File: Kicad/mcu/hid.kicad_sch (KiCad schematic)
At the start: 34 parts, among them IC401 MCP2221A, K401 VIN, K402 FRONT #1, K403 +5V, K404 FRONT #2, K405 SERVO LEFT, K406 USB/UART, K407 FRONT #3, K408 SERVO RIGHT, K409 FRONT #4

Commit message: TBOT MCU
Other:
- note added: "*R407, *R412: Optional, for SHARP IR Wheel"
- note removed: "*R408, *R413: Optional, for SHARP IR Wheel"
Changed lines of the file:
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@@
     (effects (font (size 1.27 1.27)) (justify right bottom))
   )
-  (text "*" (at 241.3 113.03 0)
+  (text "*" (at 236.855 101.6 0)
     (effects (font (size 1.27 1.27)) (justify left bottom))
   )
@@
     (effects (font (size 1.27 1.27)) (justify right bottom))
   )
-  (text "*" (at 180.34 113.03 0)
+  (text "*" (at 175.895 101.6 0)
     (effects (font (size 1.27 1.27)) (justify left bottom))
   )
@@
     (effects (font (size 1.27 1.27)) (justify right bottom))
   )
-  (text "*R408, *R413: Optional, for SHARP IR Wheel" (at 185.42 173.99 0)
+  (text "*R407, *R412: Optional, for SHARP IR Wheel" (at 185.42 173.99 0)
     (effects (font (size 1.27 1.27)) (justify left bottom))
   )
@@
   (symbol (lib_id "tronixio:R-1206") (at 243.84 114.3 270) (unit 1)
     (in_bom yes) (on_board yes)
-    (property "Reference" "R413" (id 0) (at 244.475 111.76 90)
+    (property "Reference" "R413" (id 0) (at 243.84 111.76 90)
       (effects (font (size 1.15 1.15)))
     )
@@
   (symbol (lib_id "tronixio:R-1206") (at 236.22 104.14 180) (unit 1)
     (in_bom yes) (on_board yes)
-    (property "Reference" "R412" (id 0) (at 238.76 100.33 0)
+    (property "Reference" "R412" (id 0) (at 240.03 100.33 0)
       (effects (font (size 1.15 1.15)))
     )
@@
   (symbol (lib_id "tronixio:R-1206") (at 175.26 104.14 180) (unit 1)
     (in_bom yes) (on_board yes)
-    (property "Reference" "R407" (id 0) (at 177.8 100.33 0)
+    (property "Reference" "R407" (id 0) (at 179.07 100.33 0)
       (effects (font (size 1.15 1.15)))
     )
@@
   (symbol (lib_id "tronixio:R-1206") (at 182.88 114.3 270) (unit 1)
     (in_bom yes) (on_board yes)
-    (property "Reference" "R408" (id 0) (at 183.515 111.76 90)
-      (effects (font (size 1.15 1.15)))
-    )
+    (property "Reference" "R408" (id 0) (at 182.88 111.76 90)
+      (effects (font (size 1.15 1.15)))
+    )

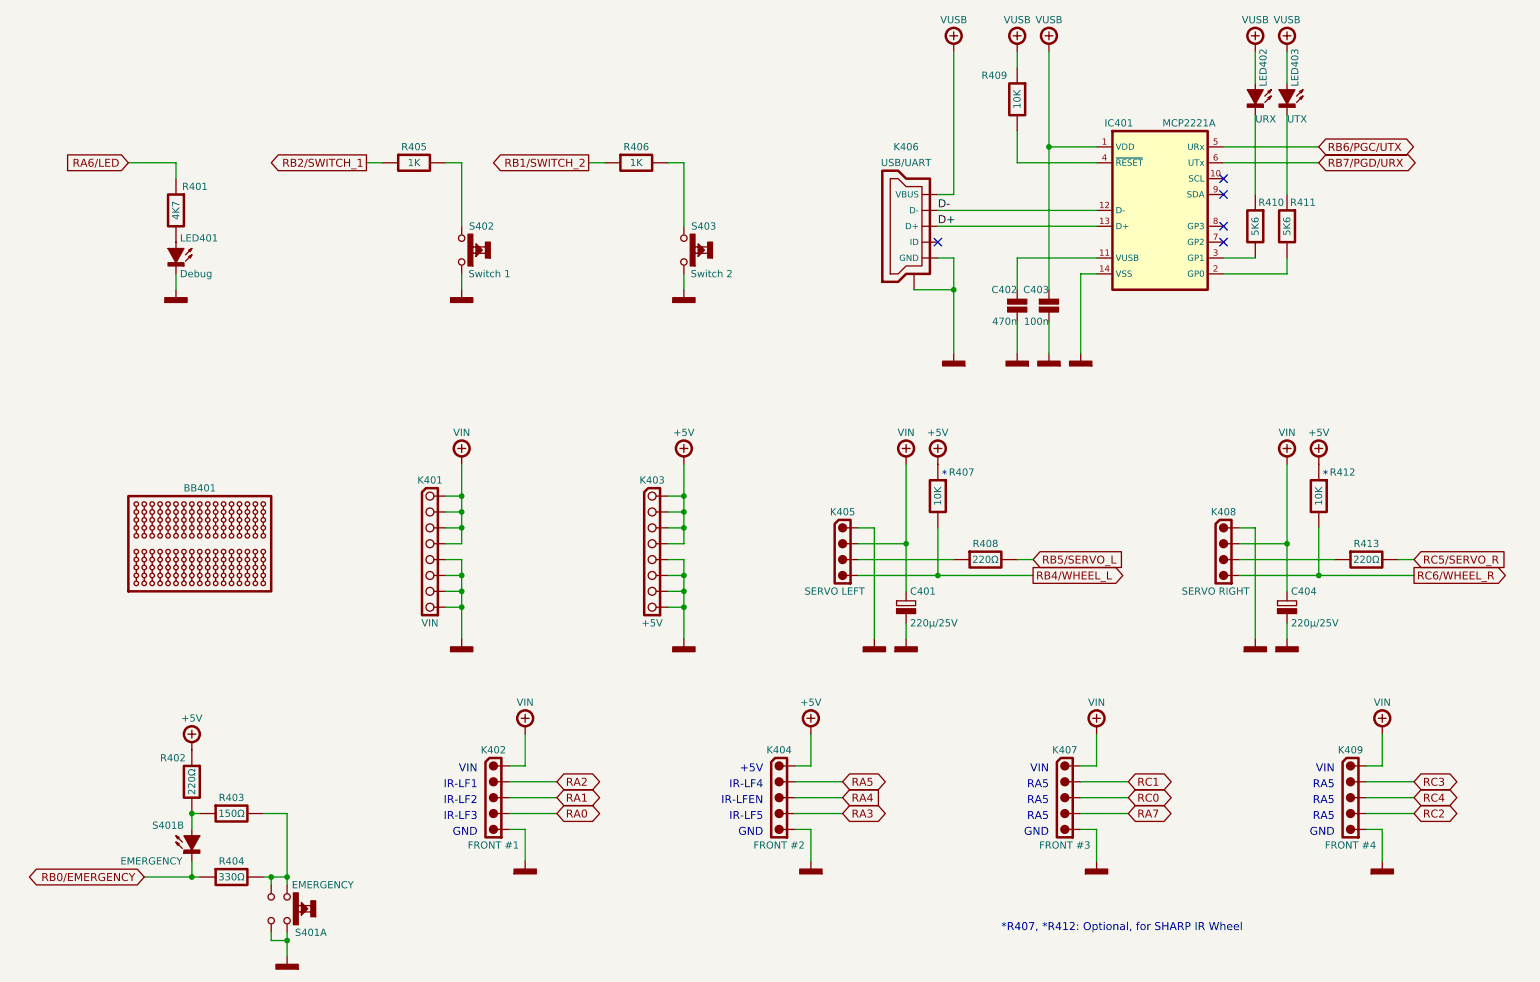
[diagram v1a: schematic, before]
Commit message: Update MCU 8Bit
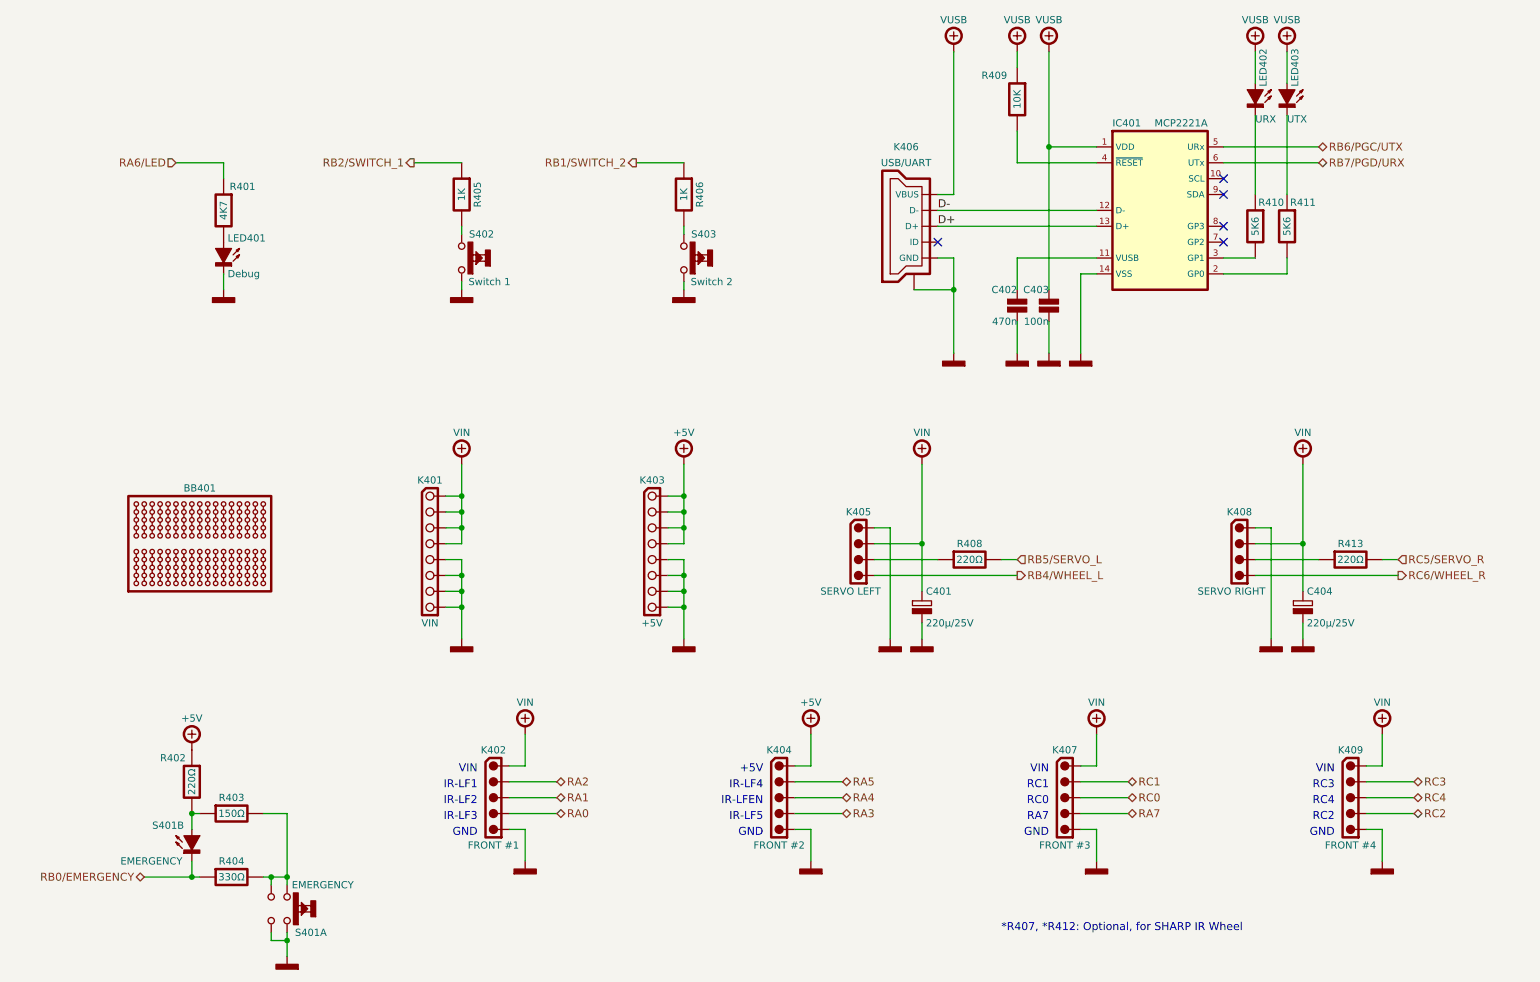
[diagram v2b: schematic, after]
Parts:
- removed R407, R412: 10K, tronixio:RESISTOR-1206, symbol tronixio:R-1206
- K401, K403: footprint tronixio:zzHARWIN-M20-782084x -> tronixio:HARWIN-M20-782084x
- K402, K404, K407, K409: footprint tronixio:zzMOLEX-532530570 -> tronixio:MOLEX-532530570
- S401: footprint tronixio:zzzE-SWITCH-TL1240XQ1JXXX -> tronixio:E-SWITCH-TL1240XQ1JXXX
- S402, S403: footprint tronixio:zzzCK-PTS635S-TH -> tronixio:CK-PTS635S-TH
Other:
- note added: "RA7"
- note added: "RC0"
- note added: "RC1"
- note added: "RC2"
- note added: "RC3"
- note added: "RC4"
- note removed: "*"
- note removed: "RA5"
- moved on the sheet: C401, C404, K405, K408, LED401, R401, R405, R406, R408, R413, S402, S403

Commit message: Update MCU
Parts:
- removed K409: FRONT #4, tronixio:MOLEX-532530570, symbol tronixio:MOLEX-MICRO-LATCH-05-VERTICAL
- removed R405, R406: 1K, tronixio:RESISTOR-1206, symbol tronixio:R-1206
- removed S402: Switch 1, tronixio:CK-PTS635S-TH, symbol tronixio:CK-PTS635-50-TH
- removed S403: Switch 2, tronixio:CK-PTS635S-TH, symbol tronixio:CK-PTS635-50-TH
- LED401, LED402, LED403: symbol tronixio:LED-1206-RED -> tronixio:LED-1206-PURPLE
- R407: renamed from R410; value 5K6 -> 4K7
- R409: renamed from R411; value 5K6 -> 4K7
- renumbered K402 to K401, K404 to K402, K401 to K403, K403 to K404, K407 to K405, K405 to K406, K406 to K407, R402 to R401, R403 to R402, R404 to R403, R401 to R404, R408 to R405, R409 to R406, R413 to R408
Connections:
- net RA7 is gone; now on net RC0: K405.4
- net RC0: no longer K405.3
- net RC1: now also K405.3; no longer K405.2
- net RC2: now also K405.2
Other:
- note added: "IR WHEEL"
- note added: "SERVO"
- note removed: "*R407, *R412: Optional, for SHARP IR Wheel"
- note removed: "RA7"
- note removed: "RC3"
- note removed: "RC4"
- moved on the sheet: BB401, C401, C402, C403, C404, IC401, K401, K402, K403, K404, K405, K406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
